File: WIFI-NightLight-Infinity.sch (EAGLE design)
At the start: 55 parts, among them CN1 PBS-3-VERTICAL, CN2 PBS-2-VERTICAL, CN5 PBS-2-VERTICAL, CN6 PBS-2-VERTICAL, CN7 PBS-4-VERTICAL, IC3 MC34063AD, IC4 DS1307Z, M1 ESP8266-12F, Q1 32.768K, T2 BC847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

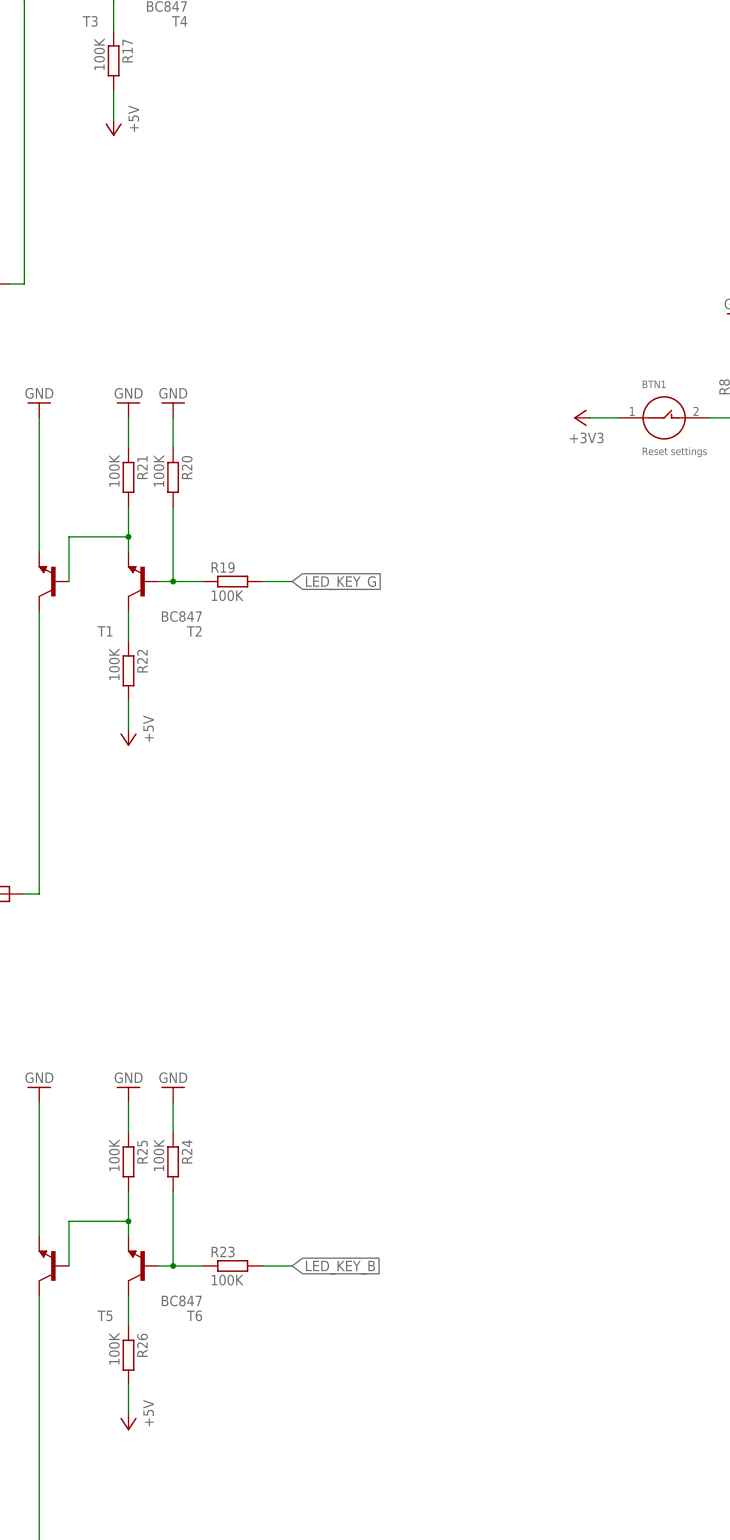
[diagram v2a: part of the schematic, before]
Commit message: Resistor was added for plus of LED-strip
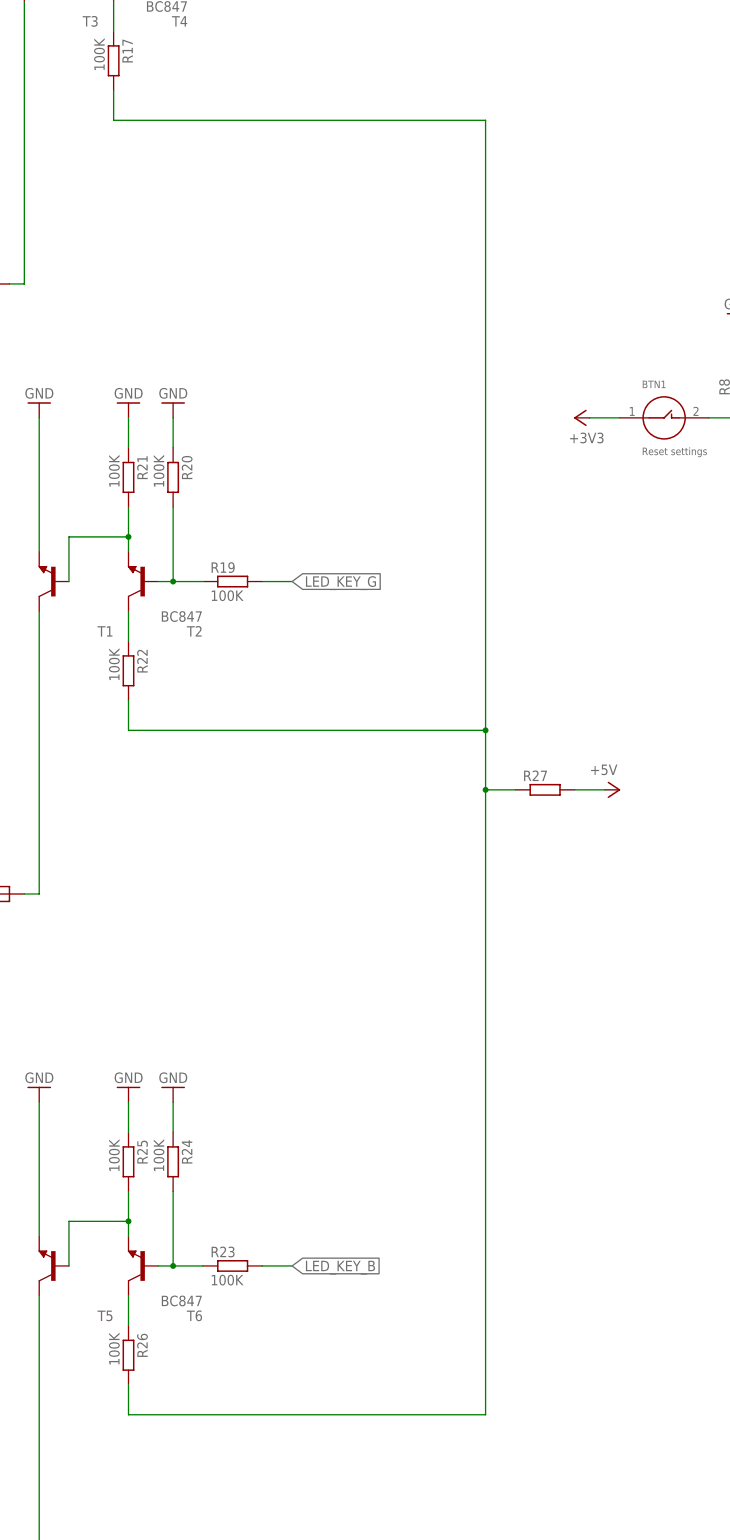
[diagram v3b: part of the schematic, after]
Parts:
- added R27: (no value), resistor:R-EU_0411/12
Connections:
- new net N$21: R17.2, R22.2, R26.2, R27.1
- net +5V: now also R27.2; no longer R17.2, R22.2, R26.2
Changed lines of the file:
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@@
 <part name="GND22" library="supply1" library_urn="urn:adsk.eagle:library:371" deviceset="GND" device=""/>
 <part name="R17" library="eagle-ltspice" library_urn="urn:adsk.eagle:library:217" deviceset="R" device="R0603" package3d_urn="urn:adsk.eagle:package:13302/1" value="100K"/>
-<part name="P+5" library="supply1" library_urn="urn:adsk.eagle:library:371" deviceset="+5V" device=""/>
 <part name="CN3" library="pls" deviceset="PBS-1-VERTICAL" device=""/>
 <part name="T1" library="transistor" library_urn="urn:adsk.eagle:library:402" deviceset="*-NPN-" device="TO126V" package3d_urn="urn:adsk.eagle:package:29912/1"/>
@@
 <part name="GND25" library="supply1" library_urn="urn:adsk.eagle:library:371" deviceset="GND" device=""/>
 <part name="R22" library="eagle-ltspice" library_urn="urn:adsk.eagle:library:217" deviceset="R" device="R0603" package3d_urn="urn:adsk.eagle:package:13302/1" value="100K"/>
-<part name="P+4" library="supply1" library_urn="urn:adsk.eagle:library:371" deviceset="+5V" device=""/>
 <part name="CN4" library="pls" deviceset="PBS-1-VERTICAL" device=""/>
 <part name="T5" library="transistor" library_urn="urn:adsk.eagle:library:402" deviceset="*-NPN-" device="TO126V" package3d_urn="urn:adsk.eagle:package:29912/1"/>
@@
 <part name="GND28" library="supply1" library_urn="urn:adsk.eagle:library:371" deviceset="GND" device=""/>
 <part name="R26" library="eagle-ltspice" library_urn="urn:adsk.eagle:library:217" deviceset="R" device="R0603" package3d_urn="urn:adsk.eagle:package:13302/1" value="100K"/>
-<part name="P+6" library="supply1" library_urn="urn:adsk.eagle:library:371" deviceset="+5V" device=""/>
 <part name="CN8" library="pls" deviceset="PBS-1-VERTICAL" device=""/>
+<part name="R27" library="resistor" library_urn="urn:adsk.eagle:library:348" deviceset="R-EU_" device="0411/12" package3d_urn="urn:adsk.eagle:package:26091/1"/>
+<part name="P+7" library="supply1" library_urn="urn:adsk.eagle:library:371" deviceset="+5V" device=""/>
 </parts>
 <sheets>
@@
 <instance part="GND22" gate="1" x="-177.8" y="48.26" rot="R180"/>
 <instance part="R17" gate="G$1" x="-177.8" y="2.54" rot="R270"/>
-<instance part="P+5" gate="1" x="-177.8" y="-10.16" rot="R180"/>
 <instance part="CN3" gate="G$1" x="-200.66" y="-35.56"/>
 <instance part="T1" gate="G$1" x="-187.96" y="-86.36" rot="R180"/>
@@
 <instance part="GND25" gate="1" x="-175.26" y="-55.88" rot="R180"/>
 <instance part="R22" gate="G$1" x="-175.26" y="-101.6" rot="R270"/>
-<instance part="P+4" gate="1" x="-175.26" y="-114.3" rot="R180"/>
 <instance part="CN4" gate="G$1" x="-198.12" y="-139.7"/>
 <instance part="T5" gate="G$1" x="-187.96" y="-203.2" rot="R180"/>
@@
 <instance part="GND28" gate="1" x="-175.26" y="-172.72" rot="R180"/>
 <instance part="R26" gate="G$1" x="-175.26" y="-218.44" rot="R270"/>
-<instance part="P+6" gate="1" x="-175.26" y="-231.14" rot="R180"/>
 <instance part="CN8" gate="G$1" x="-198.12" y="-256.54"/>
+<instance part="R27" gate="G$1" x="-104.14" y="-121.92"/>
+<instance part="P+7" gate="1" x="-91.44" y="-121.92" rot="R270"/>
 </instances>
 <busses>
@@
 </segment>
 <segment>
-<pinref part="R17" gate="G$1" pin="2"/>
-<pinref part="P+5" gate="1" pin="+5V"/>
-<wire x1="-177.8" y1="-7.62" x2="-177.8" y2="-2.54" width="0.1524" layer="91"/>
-</segment>
-<segment>
-<pinref part="R22" gate="G$1" pin="2"/>
-<pinref part="P+4" gate="1" pin="+5V"/>
-<wire x1="-175.26" y1="-111.76" x2="-175.26" y2="-106.68" width="0.1524" layer="91"/>
-</segment>
-<segment>
-<pinref part="R26" gate="G$1" pin="2"/>
-<pinref part="P+6" gate="1" pin="+5V"/>
-<wire x1="-175.26" y1="-228.6" x2="-175.26" y2="-223.52" width="0.1524" layer="91"/>
+<pinref part="R27" gate="G$1" pin="2"/>
+<pinref part="P+7" gate="1" pin="+5V"/>
+<wire x1="-93.98" y1="-121.92" x2="-99.06" y2="-121.92" width="0.1524" layer="91"/>
 </segment>
 </net>
@@
 </segment>
 </net>
+<net name="N$21" class="0">
+<segment>
+<pinref part="R26" gate="G$1" pin="2"/>
+<wire x1="-175.26" y1="-228.6" x2="-175.26" y2="-223.52" width="0.1524" layer="91"/>
+<pinref part="R22" gate="G$1" pin="2"/>
+<wire x1="-175.26" y1="-111.76" x2="-175.26" y2="-106.68" width="0.1524" layer="91"/>
+<pinref part="R17" gate="G$1" pin="2"/>
+<wire x1="-177.8" y1="-7.62" x2="-177.8" y2="-2.54" width="0.1524" layer="91"/>
+<pinref part="R27" gate="G$1" pin="1"/>
+<wire x1="-109.22" y1="-121.92" x2="-114.3" y2="-121.92" width="0.1524" layer="91"/>
+<wire x1="-114.3" y1="-121.92" x2="-114.3" y2="-228.6" width="0.1524" layer="91"/>
+<wire x1="-114.3" y1="-121.92" x2="-114.3" y2="-111.76" width="0.1524" layer="91"/>
+<junction x="-114.3" y="-121.92"/>
+<wire x1="-114.3" y1="-111.76" x2="-114.3" y2="-7.62" width="0.1524" layer="91"/>
+<wire x1="-177.8" y1="-7.62" x2="-114.3" y2="-7.62" width="0.1524" layer="91"/>
+<wire x1="-175.26" y1="-111.76" x2="-114.3" y2="-111.76" width="0.1524" layer="91"/>
+<junction x="-114.3" y="-111.76"/>
+<wire x1="-175.26" y1="-228.6" x2="-114.3" y2="-228.6" width="0.1524" layer="91"/>
+</segment>
+</net>

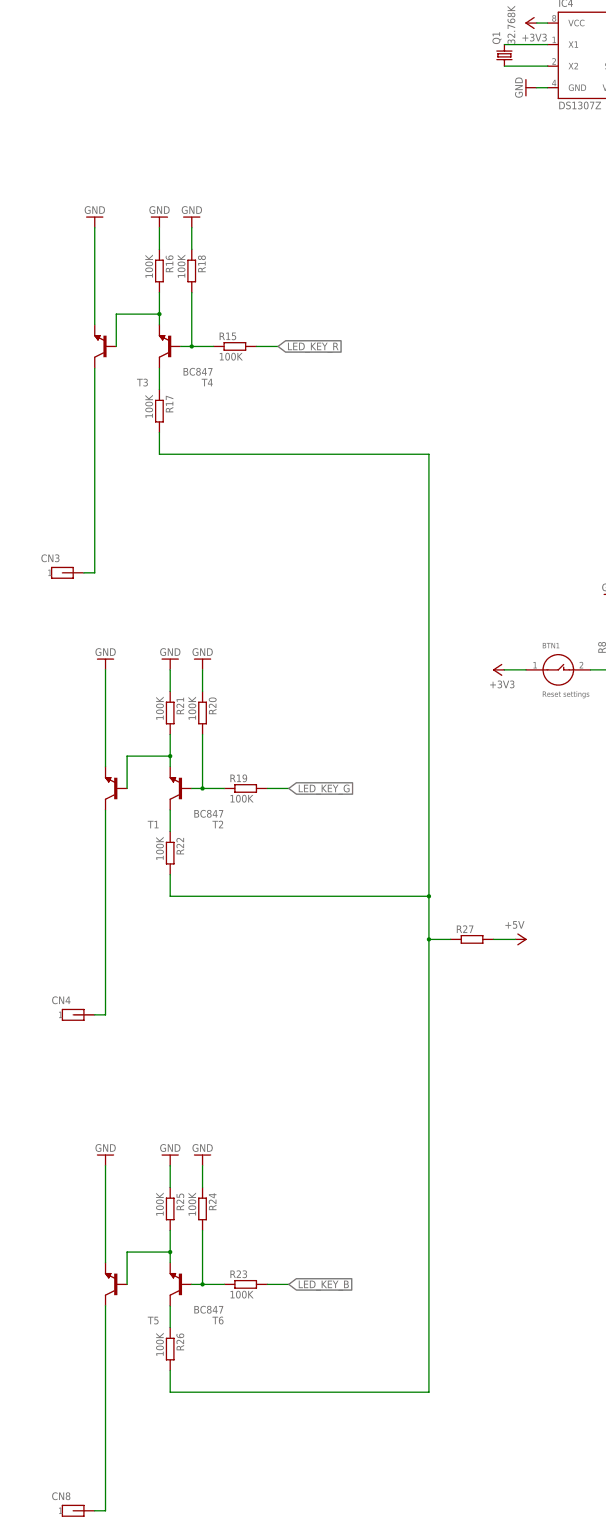
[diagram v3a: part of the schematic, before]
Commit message: Errors were fixed
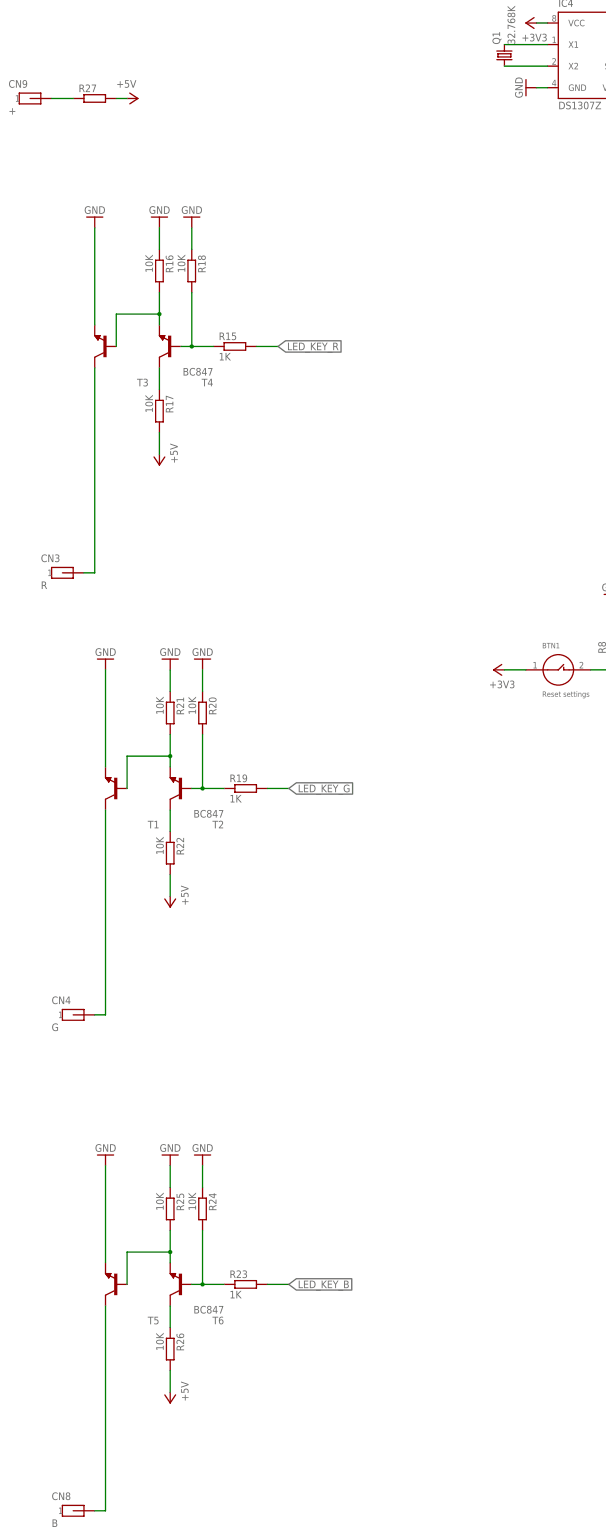
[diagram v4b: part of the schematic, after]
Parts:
- added CN9: +, pls:PBS-1-VERTICAL
- CN3: value (none) -> R
- CN4: value (none) -> G
- CN8: value (none) -> B
- R15, R19, R23: value 100K -> 1K
- R16, R17, R18, R20, R21, R22, R24, R25, R26: value 100K -> 10K
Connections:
- removed net N$21: R17.2, R22.2, R26.2, R27.1
- new net N$20: CN9.1, R27.1
- net +5V: now also R17.2, R22.2, R26.2
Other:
- moved on the sheet: R27

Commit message: Value was changed. Updating for Eagle 9.2.0
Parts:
- R10: value 5.1k -> 5.6k
- R27: value (none) -> 56
